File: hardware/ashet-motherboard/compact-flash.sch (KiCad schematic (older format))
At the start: 7 parts

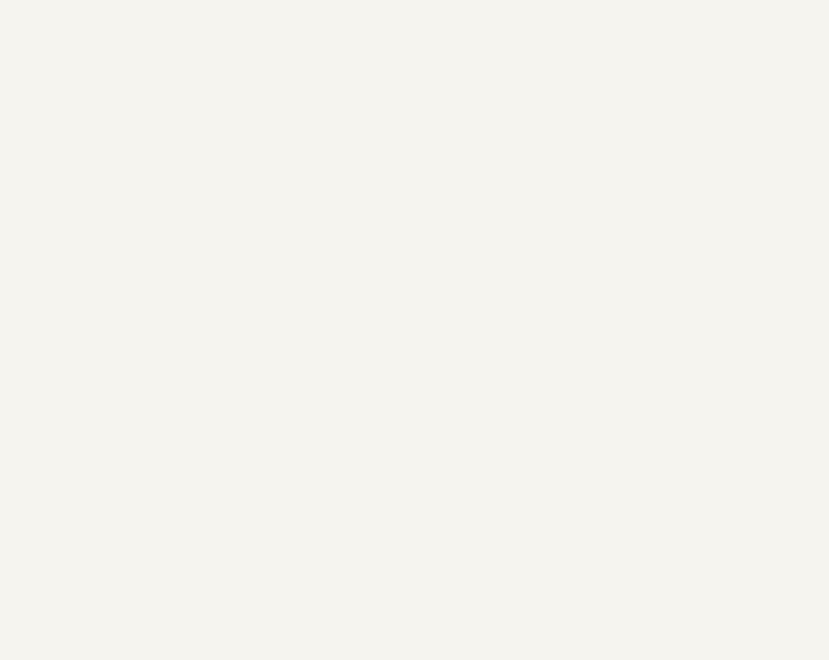
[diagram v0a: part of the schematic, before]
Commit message: schematics for pcm audio and ps/2.
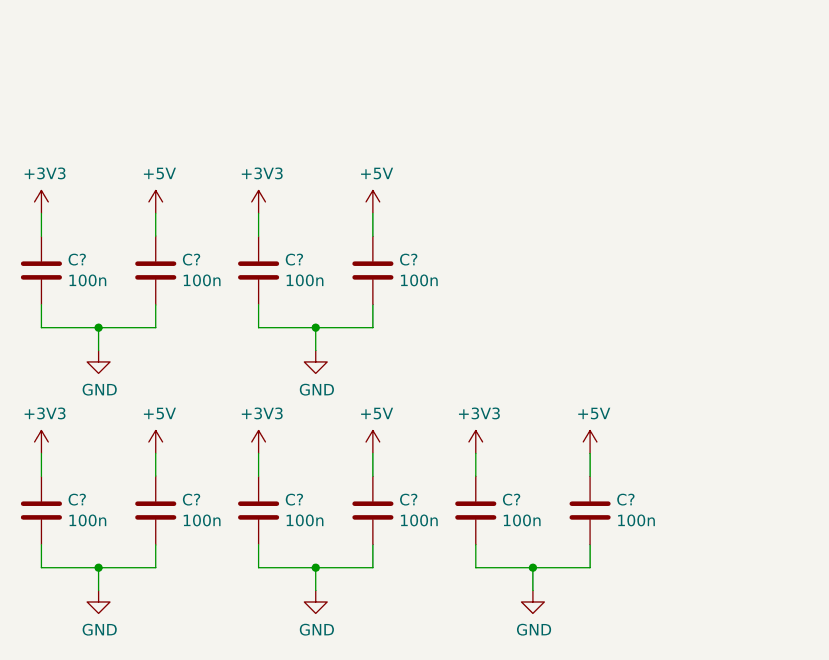
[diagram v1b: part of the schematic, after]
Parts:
- added C? (x10): 100n, symbol Device:C
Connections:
- net +3V3: now also C?.1, C?.1, C?.1, C?.1, C?.1
- net +5V: now also C?.1, C?.1, C?.1, C?.1, C?.1
- net GND: now also C?.2, C?.2, C?.2, C?.2, C?.2, C?.2, C?.2, C?.2, C?.2, C?.2
